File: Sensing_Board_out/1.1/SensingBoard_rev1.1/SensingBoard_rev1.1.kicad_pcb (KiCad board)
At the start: 4 copper layers, 40 x 40 mm, 89 parts, among them J1 USB_C_Receptacle, J2 3221-10-0300-00, J3 F32R-1A7H1-11024, J5 RS1-02-G, J6 RS1-02-G, J7 RS1-02-G, J9 RS1-02-G, SW1 PTS815 SJM 250 SMTR LFS, SW2 PTS815 SJM 250 SMTR LFS, U2 BNO055, U3 MIC5504-3.3YM5, U4 FT232RQ, U5 MIC5504-1.8YM5, U6 MCP1700x-280xxTT, U7 ESP32-S3, U8 GD25D05CT, Y1 ABM8G-40.000MHZ-18-D2Y-T

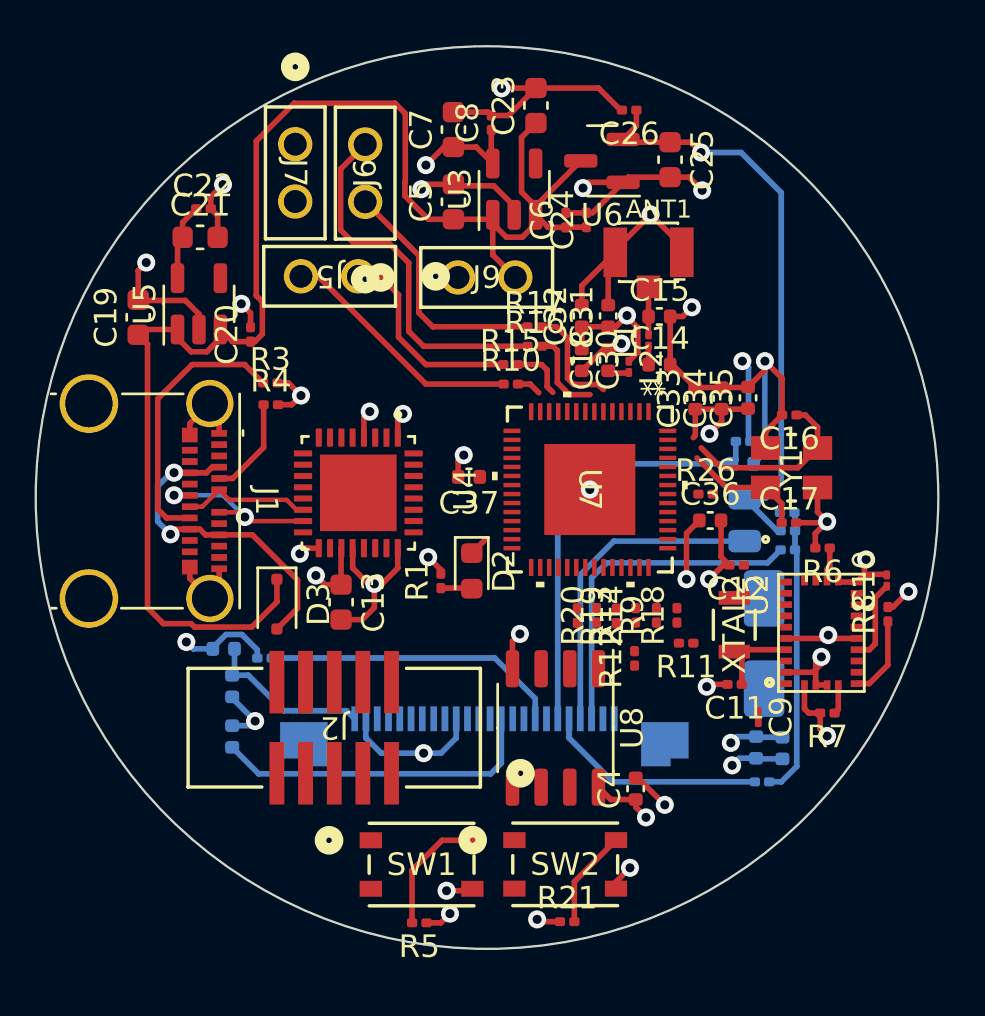
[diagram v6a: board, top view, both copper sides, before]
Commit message: sense board layout
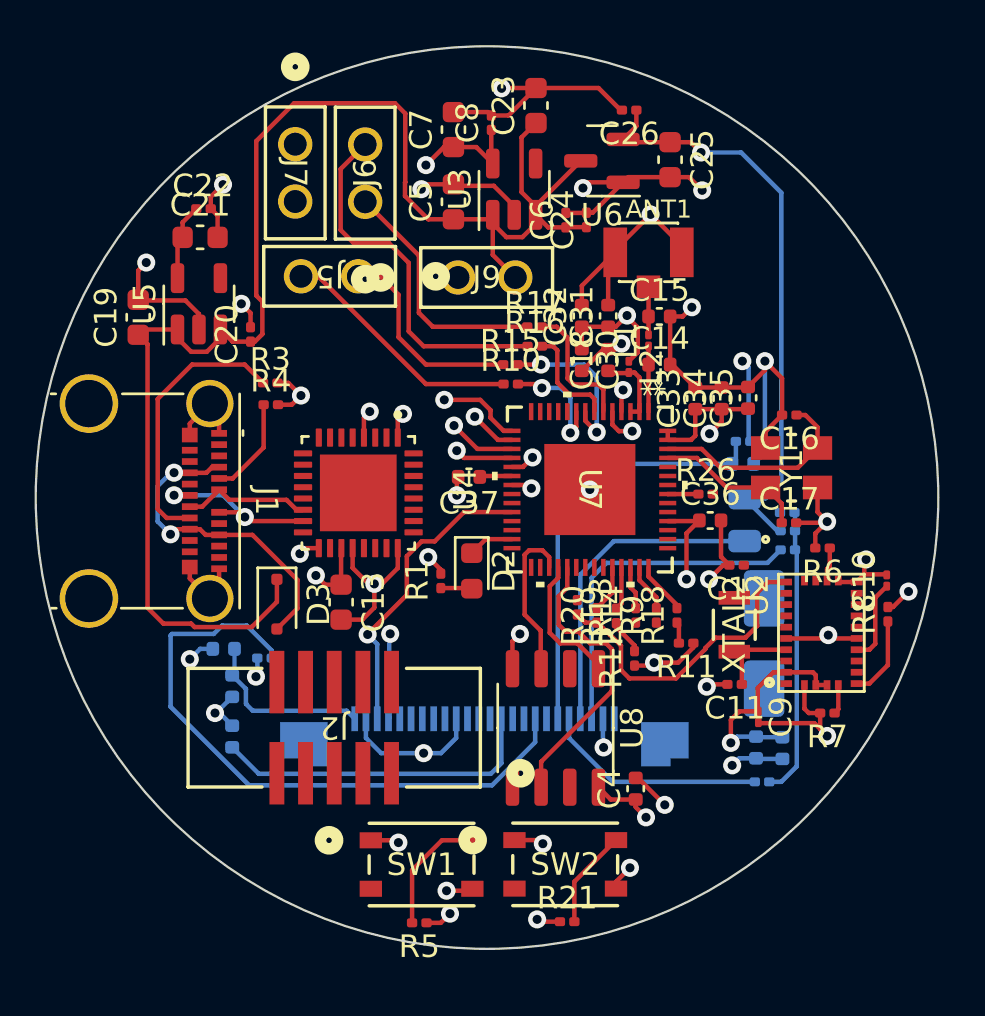
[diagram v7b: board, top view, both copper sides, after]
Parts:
- moved R13 0.37 mm to (134.2, 67.4)
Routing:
- net Net-(J3-Pad8): track 13.3 -> 28.0 mm
- net BNO_SDA: track 0.00 -> 13.7 mm
- net IO18/DVP_Y4: track 0.00 -> 13.6 mm, vias 0 -> 1
- net SPICLK: track 0.00 -> 12.9 mm
- net +3.3V: track 38.7 -> 49.6 mm
- net SPIWP: track 0.00 -> 7.11 mm
- net SPICS0: track 0.00 -> 5.98 mm
- net D2/A2: track 2.50 -> 7.36 mm, vias 0 -> 2
- net D3/A3: track 1.08 -> 5.18 mm, vias 0 -> 2
- net IO17/DVP_Y3: track 0.00 -> 3.80 mm, vias 0 -> 1
- net IO10/XMCLK: track 0.00 -> 3.77 mm, vias 0 -> 1
- net IO12/DVP_Y7: track 0.00 -> 3.00 mm, vias 0 -> 1
- net GPIO0: track 0.00 -> 2.90 mm, vias 0 -> 2
- net IO13/DVP_PCLK: track 0.00 -> 2.58 mm, vias 0 -> 1
- net Net-(C18-Pad1): track 0.87 -> 3.34 mm
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
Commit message: updates
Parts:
- moved R13 6.12 mm to (137.8, 72.3), turned to 0 degrees
- moved R20 4.62 mm to (137.8, 71.4), turned to 180 degrees
- moved R12 0.71 mm to (137.4, 69.6), turned to 180 degrees
- moved R11 0.50 mm to (138.6, 69.2), turned to 90 degrees
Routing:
- net +1V8: track 3.42 -> 44.2 mm, vias 0 -> 2
- net DRV_FAULT: track 0.95 -> 40.3 mm, vias 0 -> 1
- net DRV_SLEEP: track 0.00 -> 38.3 mm, vias 0 -> 1
- net CHIP_EN: track 2.25 -> 29.2 mm
- net GPIO0: track 2.90 -> 23.3 mm
- net TX_D6: track 0.00 -> 19.2 mm, vias 0 -> 2
- net IO38/DVP_VSYNC: track 0.00 -> 17.9 mm, vias 0 -> 2
- net IO10/XMCLK: track 3.77 -> 21.0 mm
- net SPID: track 0.00 -> 16.1 mm, vias 0 -> 2
- net +2V8: track 41.1 -> 56.1 mm, vias 1 -> 3
- net RX_D7: track 0.00 -> 14.4 mm, vias 0 -> 2
- net BNO_SCL: track 1.58 -> 13.9 mm
- net IO47/DVP_HREF: track 0.00 -> 12.2 mm, vias 0 -> 2
- net IO48/DVP_Y9: track 0.00 -> 11.5 mm, vias 0 -> 2
- net MTCK/IO39/CAM_SCL: track 9.89 -> 21.3 mm, vias 0 -> 1
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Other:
- copper layers 4 -> 6
